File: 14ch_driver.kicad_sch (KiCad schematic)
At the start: 4 parts, among them U1 ULN2003, U2 74HC595, U3 74HC595, U4 ULN2003

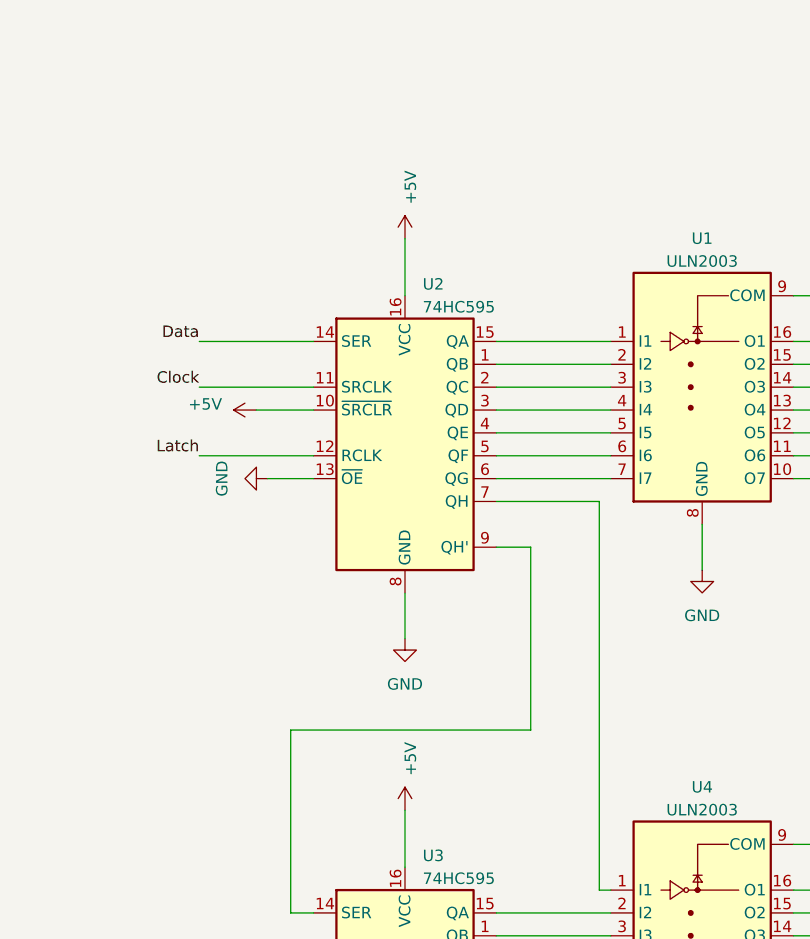
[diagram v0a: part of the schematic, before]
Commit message: Finished up schematic, before board splitting
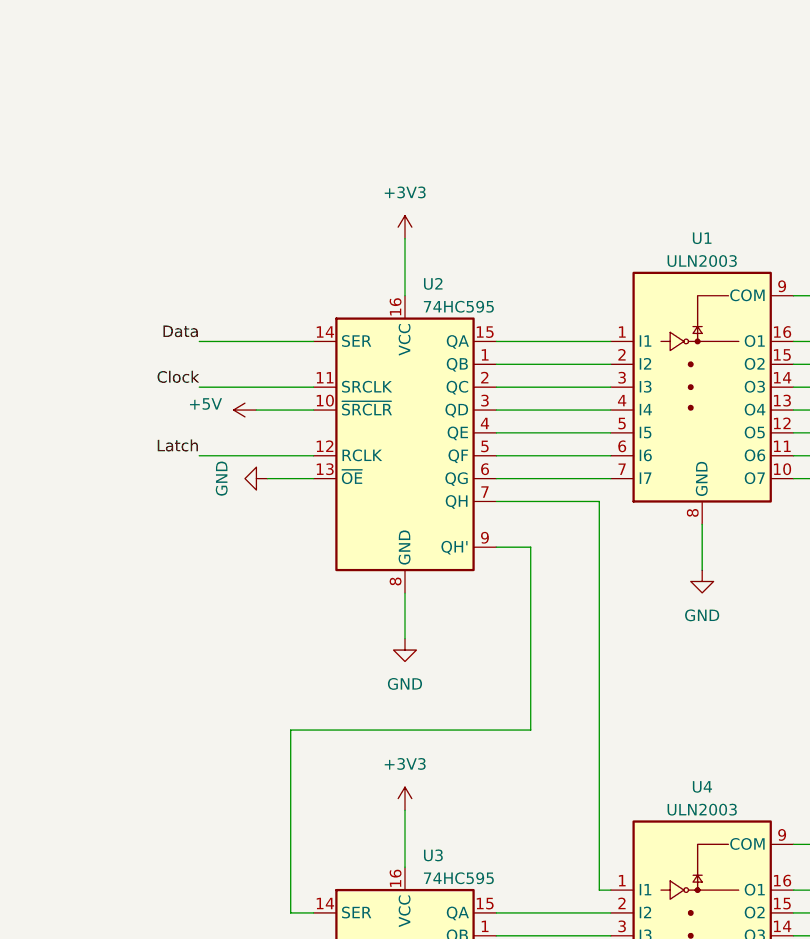
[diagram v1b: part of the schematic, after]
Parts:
- U1, U2, U3, U4: footprint (none) -> Package_SO:SOIC-16_3.9x9.9mm_P1.27mm
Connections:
- net +5V: no longer U2.16 (VCC), U3.16 (VCC)
- new net +3V3: U2.16 (VCC), U3.16 (VCC)
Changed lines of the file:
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@@
       (effects (font (size 1.27 1.27)))
     )
-    (property "Footprint" "" (at 180.34 133.35 0)
+    (property "Footprint" "Package_SO:SOIC-16_3.9x9.9mm_P1.27mm" (at 180.34 133.35 0)
       (effects (font (size 1.27 1.27)) (justify left) hide)
     )
@@
     )
   )
-  (symbol (lib_id "power:+5V") (at 146.05 105.41 0) (unit 1)
-    (in_bom yes) (on_board yes) (dnp no) (fields_autoplaced)
-    (property "Reference" "#PWR018" (at 146.05 109.22 0)
-      (effects (font (size 1.27 1.27)) hide)
-    )
-    (property "Value" "+5V" (at 146.685 101.6 90)
-      (effects (font (size 1.27 1.27)) (justify left))
-    )
-    (property "Footprint" "" (at 146.05 105.41 0)
-      (effects (font (size 1.27 1.27)) hide)
-    )
-    (property "Datasheet" "" (at 146.05 105.41 0)
-      (effects (font (size 1.27 1.27)) hide)
-    )
-    (pin "1")
-    (instances
-      (project "EF_matrix"
-        (path "/621f65ee-d66d-40b7-9a89-3052b9373190"
+  (symbol (lib_id "power:GND") (at 179.07 78.74 0) (unit 1)
+    (in_bom yes) (on_board yes) (dnp no) (fields_autoplaced)
+    (property "Reference" "#PWR01" (at 179.07 85.09 0)
+      (effects (font (size 1.27 1.27)) hide)
+    )
+    (property "Value" "GND" (at 179.07 83.82 0)
+      (effects (font (size 1.27 1.27)))
+    )
+    (property "Footprint" "" (at 179.07 78.74 0)
+      (effects (font (size 1.27 1.27)) hide)
+    )
+    (property "Datasheet" "" (at 179.07 78.74 0)
+      (effects (font (size 1.27 1.27)) hide)
+    )
+    (pin "1")
+    (instances
+      (project "EF_matrix"
+        (path "/621f65ee-d66d-40b7-9a89-3052b9373190"
+          (reference "#PWR01") (unit 1)
+        )
+        (path "/621f65ee-d66d-40b7-9a89-3052b9373190/52ee115b-1e62-43a1-aac1-0de0837e1c5b"
           (reference "#PWR018") (unit 1)
         )
-        (path "/621f65ee-d66d-40b7-9a89-3052b9373190/52ee115b-1e62-43a1-aac1-0de0837e1c5b"
-          (reference "#PWR016") (unit 1)
-        )
-      )
-    )
-  )
-  (symbol (lib_id "power:GND") (at 179.07 78.74 0) (unit 1)
-    (in_bom yes) (on_board yes) (dnp no) (fields_autoplaced)
-    (property "Reference" "#PWR01" (at 179.07 85.09 0)
-      (effects (font (size 1.27 1.27)) hide)
-    )
-    (property "Value" "GND" (at 179.07 83.82 0)
-      (effects (font (size 1.27 1.27)))
-    )
-    (property "Footprint" "" (at 179.07 78.74 0)
-      (effects (font (size 1.27 1.27)) hide)
-    )
-    (property "Datasheet" "" (at 179.07 78.74 0)
-      (effects (font (size 1.27 1.27)) hide)
-    )
-    (pin "1")
-    (instances
-      (project "EF_matrix"
-        (path "/621f65ee-d66d-40b7-9a89-3052b9373190"
-          (reference "#PWR01") (unit 1)
-        )
-        (path "/621f65ee-d66d-40b7-9a89-3052b9373190/52ee115b-1e62-43a1-aac1-0de0837e1c5b"
-          (reference "#PWR018") (unit 1)
-        )
       )
     )
@@
     )
   )
+  (symbol (lib_id "power:+3V3") (at 146.05 41.91 0) (unit 1)
+    (in_bom yes) (on_board yes) (dnp no) (fields_autoplaced)
+    (property "Reference" "#PWR05" (at 146.05 45.72 0)
+      (effects (font (size 1.27 1.27)) hide)
+    )
+    (property "Value" "+3V3" (at 146.05 36.83 0)
+      (effects (font (size 1.27 1.27)))
+    )
+    (property "Footprint" "" (at 146.05 41.91 0)
+      (effects (font (size 1.27 1.27)) hide)
+    )
+    (property "Datasheet" "" (at 146.05 41.91 0)
+      (effects (font (size 1.27 1.27)) hide)
+    )
+    (pin "1")
+    (instances
+      (project "EF_matrix"
+        (path "/621f65ee-d66d-40b7-9a89-3052b9373190/52ee115b-1e62-43a1-aac1-0de0837e1c5b"
+          (reference "#PWR05") (unit 1)
+        )
+      )
+    )
+  )
   (symbol (lib_id "power:GND") (at 146.05 149.86 0) (unit 1)
     (in_bom yes) (on_board yes) (dnp no) (fields_autoplaced)
@@
       (effects (font (size 1.27 1.27)) (justify left))
     )
-    (property "Footprint" "" (at 146.05 63.5 0)
+    (property "Footprint" "Package_SO:SOIC-16_3.9x9.9mm_P1.27mm" (at 146.05 63.5 0)
       (effects (font (size 1.27 1.27)) hide)
     )
@@
       (effects (font (size 1.27 1.27)) (justify left))
     )
-    (property "Footprint" "" (at 146.05 127 0)
+    (property "Footprint" "Package_SO:SOIC-16_3.9x9.9mm_P1.27mm" (at 146.05 127 0)
       (effects (font (size 1.27 1.27)) hide)
     )
@@
     )
   )
+  (symbol (lib_id "power:+3V3") (at 146.05 105.41 0) (unit 1)
+    (in_bom yes) (on_board yes) (dnp no) (fields_autoplaced)
+    (property "Reference" "#PWR016" (at 146.05 109.22 0)
+      (effects (font (size 1.27 1.27)) hide)
+    )
+    (property "Value" "+3V3" (at 146.05 100.33 0)
+      (effects (font (size 1.27 1.27)))
+    )
+    (property "Footprint" "" (at 146.05 105.41 0)
+      (effects (font (size 1.27 1.27)) hide)
+    )
+    (property "Datasheet" "" (at 146.05 105.41 0)
+      (effects (font (size 1.27 1.27)) hide)
+    )
+    (pin "1")
+    (instances
+      (project "EF_matrix"
+        (path "/621f65ee-d66d-40b7-9a89-3052b9373190/52ee115b-1e62-43a1-aac1-0de0837e1c5b"
+          (reference "#PWR016") (unit 1)
+        )
+      )
+    )
+  )
   (symbol (lib_id "power:GND") (at 130.81 68.58 270) (unit 1)
     (in_bom yes) (on_board yes) (dnp no) (fields_autoplaced)
@@
       (effects (font (size 1.27 1.27)))
     )
-    (property "Footprint" "" (at 180.34 72.39 0)
+    (property "Footprint" "Package_SO:SOIC-16_3.9x9.9mm_P1.27mm" (at 180.34 72.39 0)
       (effects (font (size 1.27 1.27)) (justify left) hide)
     )
@@
         )
       )
-    )
-  )
-  (symbol (lib_id "power:+5V") (at 146.05 41.91 0) (unit 1)
-    (in_bom yes) (on_board yes) (dnp no) (fields_autoplaced)
-    (property "Reference" "#PWR04" (at 146.05 45.72 0)
-      (effects (font (size 1.27 1.27)) hide)
-    )
-    (property "Value" "+5V" (at 146.685 38.1 90)
-      (effects (font (size 1.27 1.27)) (justify left))
-    )
-    (property "Footprint" "" (at 146.05 41.91 0)
-      (effects (font (size 1.27 1.27)) hide)
-    )
-    (property "Datasheet" "" (at 146.05 41.91 0)
-      (effects (font (size 1.27 1.27)) hide)
-    )
-    (pin "1")
-    (instances
-      (project "EF_matrix"
-        (path "/621f65ee-d66d-40b7-9a89-3052b9373190"
-          (reference "#PWR04") (unit 1)
-        )
-        (path "/621f65ee-d66d-40b7-9a89-3052b9373190/52ee115b-1e62-43a1-aac1-0de0837e1c5b"
-          (reference "#PWR05") (unit 1)
-        )
-      )

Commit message: Changed position of ribbon connectors, added DC
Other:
- company: (none) -> Daniel Machnik Sounddesign und Tontechnik
- title: (none) -> Essigfabrik 2-Way PA Switcher
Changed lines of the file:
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@@
 (kicad_sch (version 20230121) (generator eeschema)
   (paper "A4")
+  (title_block
+    (title "Essigfabrik 2-Way PA Switcher")
+    (date "2023-11-21")
+    (rev "1")
+    (company "Daniel Machnik Sounddesign und Tontechnik")
+  )
   (no_connect (at 156.21 134.62))
   (no_connect (at 156.21 132.08))
